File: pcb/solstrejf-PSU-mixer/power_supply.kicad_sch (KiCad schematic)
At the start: 20 parts, among them U2 L7815, U3 L7915

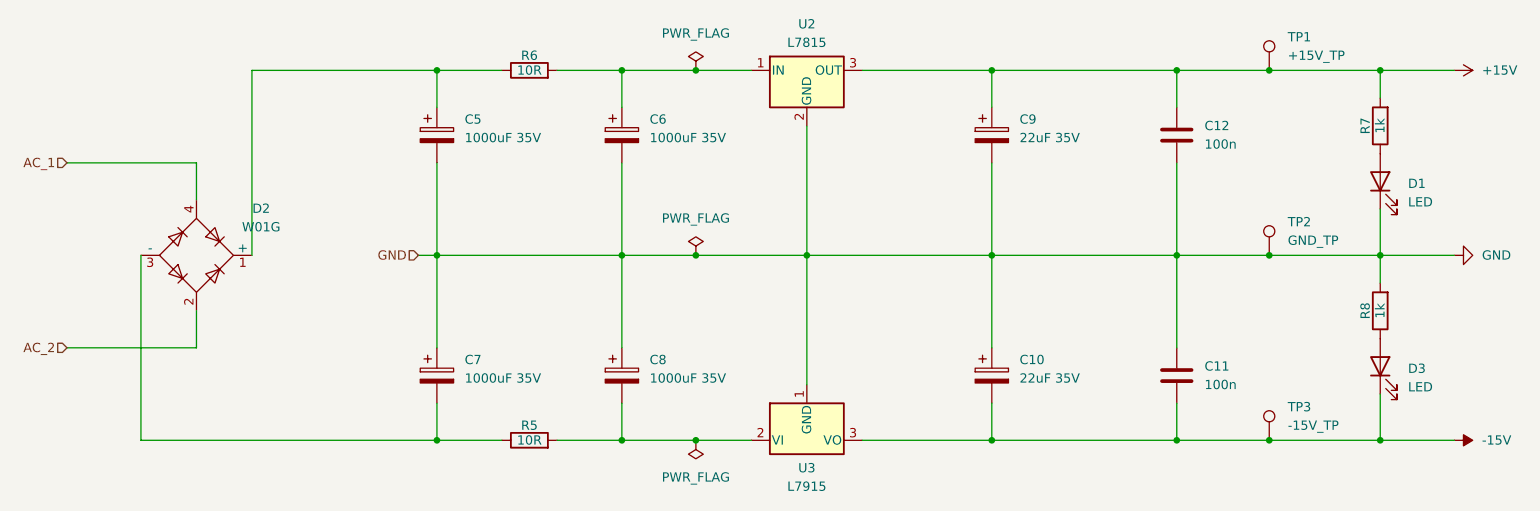
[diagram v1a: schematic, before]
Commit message: made first attempt of a PCB layout onf the PSU/mixer. No routing performed. Minor updates to schematic, including mounting holes.
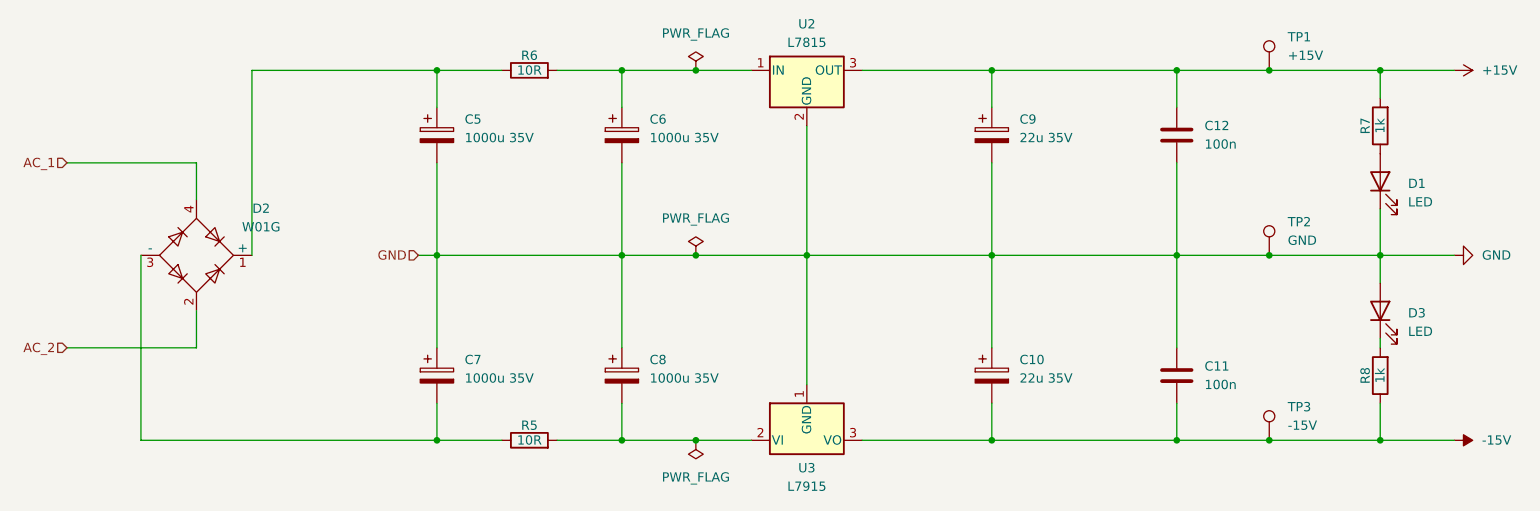
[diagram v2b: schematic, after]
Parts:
- C10, C9: value 22uF 35V -> 22u 35V
- C5, C6, C7, C8: value 1000uF 35V -> 1000u 35V
- TP1: value +15V_TP -> +15V
- TP2: value GND_TP -> GND
- TP3: value -15V_TP -> -15V
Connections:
- net -15V: now also R8.1; no longer D3.1 (K)
- net GND: now also D3.2 (A); no longer R8.2
- new net: D3.1 (K), R8.2
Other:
- moved on the sheet: D3, R8
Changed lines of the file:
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@@
+	(wire
+		(pts
+			(xy 231.14 76.2) (xy 231.14 74.93)
+		)
+		(stroke
+			(width 0)
+			(type default)
+		)
+	)
 	(wire
 		(pts
@@
 	(wire
 		(pts
-			(xy 231.14 82.55) (xy 231.14 88.9)
+			(xy 231.14 83.82) (xy 231.14 88.9)
 		)
 		(stroke
@@
 			)
 		)
-		(property "Value" "1000uF 35V"
+		(property "Value" "1000u 35V"
 			(at 105.41 47.3709 0)
 			(effects
@@
 			)
 		)
-		(property "Value" "1000uF 35V"
+		(property "Value" "1000u 35V"
 			(at 130.81 80.3909 0)
 			(effects
@@
 			)
 		)
-		(property "Value" "GND_TP"
+		(property "Value" "GND"
 			(at 218.44 61.4679 0)
 			(effects
@@
 			)
 		)
-		(property "Value" "-15V_TP"
+		(property "Value" "-15V"
 			(at 218.44 86.8679 0)
 			(effects
@@
 			)
 		)
-		(property "Value" "1000uF 35V"
+		(property "Value" "1000u 35V"
 			(at 130.81 47.3709 0)
 			(effects
@@
 	(symbol
 		(lib_id "Device:LED")
-		(at 231.14 78.74 90)
+		(at 231.14 71.12 90)
 		(unit 1)
 		(exclude_from_sim no)
@@
 		(fields_autoplaced yes)
 		(property "Reference" "D3"
-			(at 234.95 79.0574 90)
+			(at 234.95 71.4374 90)
 			(effects
 				(font
@@
 		)
 		(property "Value" "LED"
-			(at 234.95 81.5974 90)
+			(at 234.95 73.9774 90)
 			(effects
 				(font
@@
 		)
 		(property "Footprint" "LED_THT:LED_D5.0mm_FlatTop"
-			(at 231.14 78.74 0)
+			(at 231.14 71.12 0)
 			(effects
 				(font
@@
 		)
 		(property "Datasheet" "~"
-			(at 231.14 78.74 0)
+			(at 231.14 71.12 0)
 			(effects
 				(font
@@
 		)
 		(property "Description" "Light emitting diode"
-			(at 231.14 78.74 0)
+			(at 231.14 71.12 0)
 			(effects
 				(font
@@
 			)
 		)
-		(property "Value" "22uF 35V"
+		(property "Value" "22u 35V"
 			(at 181.61 47.3709 0)
 			(effects
@@
 			)
 		)
-		(property "Value" "22uF 35V"
+		(property "Value" "22u 35V"
 			(at 181.61 80.3909 0)
 			(effects
@@
 			)
 		)
-		(property "Value" "+15V_TP"
+		(property "Value" "+15V"
 			(at 218.44 36.0679 0)
 			(effects
@@
 			)
 		)
-		(property "Value" "1000uF 35V"
+		(property "Value" "1000u 35V"
 			(at 105.41 80.3909 0)
 			(effects
@@
 	(symbol
 		(lib_id "Device:R")
-		(at 231.14 71.12 180)
+		(at 231.14 80.01 180)
 		(unit 1)
 		(exclude_from_sim no)
@@
 		(dnp no)
 		(property "Reference" "R8"
-			(at 229.108 71.12 90)
+			(at 229.108 80.01 90)
 			(effects
 				(font
@@
 		)
 		(property "Value" "1k"
-			(at 231.14 71.12 90)
+			(at 231.14 80.01 90)
 			(effects
 				(font
@@
 		)
 		(property "Footprint" "Resistor_THT:R_Axial_DIN0207_L6.3mm_D2.5mm_P10.16mm_Horizontal"
-			(at 232.918 71.12 90)
+			(at 232.918 80.01 90)
 			(effects
 				(font
@@
 		)
 		(property "Datasheet" "~"
-			(at 231.14 71.12 0)
+			(at 231.14 80.01 0)
 			(effects
 				(font
@@
 		)
 		(property "Description" "Resistor"
-			(at 231.14 71.12 0)
-			(effects
-				(font
+			(at 231.14 80.01 0)
+			(effects
+				(font

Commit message: Updated fonts in PSU+mixer schematic. Added a print of the PSU+mixer schemtic in new  directory.
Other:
- title: (none) -> Linear Split Supply AC-DC Converter
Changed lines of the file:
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@@
 	(generator_version "8.0")
 	(paper "A4")
+	(title_block
+		(title "Linear Split Supply AC-DC Converter")
+		(date "2024-08-24")
+		(rev "1.0")
+	)
 	(junction
 		(at 101.6 63.5)
